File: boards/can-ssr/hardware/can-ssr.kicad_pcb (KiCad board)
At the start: 2 copper layers, 100 x 100 mm, 127 parts, among them J1 CAN IN, J2 CAN OUT, J3 ICSP, J30 MEAN WELL, J4 UART, Q1 IPB110N20N3LF, Q2 IPB110N20N3LF, Q20 2N7002, Q21 2N7002, Q22 2N7002, Q23 2N7002, Q24 2N7002, Q3 IPB110N20N3LF, Q4 IPB110N20N3LF, Q5 MMBT2907A, SW1 ADDR, U1 R-78E5.0-1.0, U10 VOM1271T, U11 VOM1271T, U12 ACS770ECB-100U-PFF-T, U2 MCP2562FD-E/P, U20 LM393B, U3 PIC18F47Q84-I/PT, U30 UCC12050DVE, U31 ISO1640DWR, U32 MCP3426A0-E/SN, U33 MCP4725A0T-E/CH, U34 MCP4725A0T-E/CH, U35 TLP222A, U36 MCP3426A1-E/SN, U40 MAX7219CWG+, U41 CC56-12SRWA, Y1 16MHz

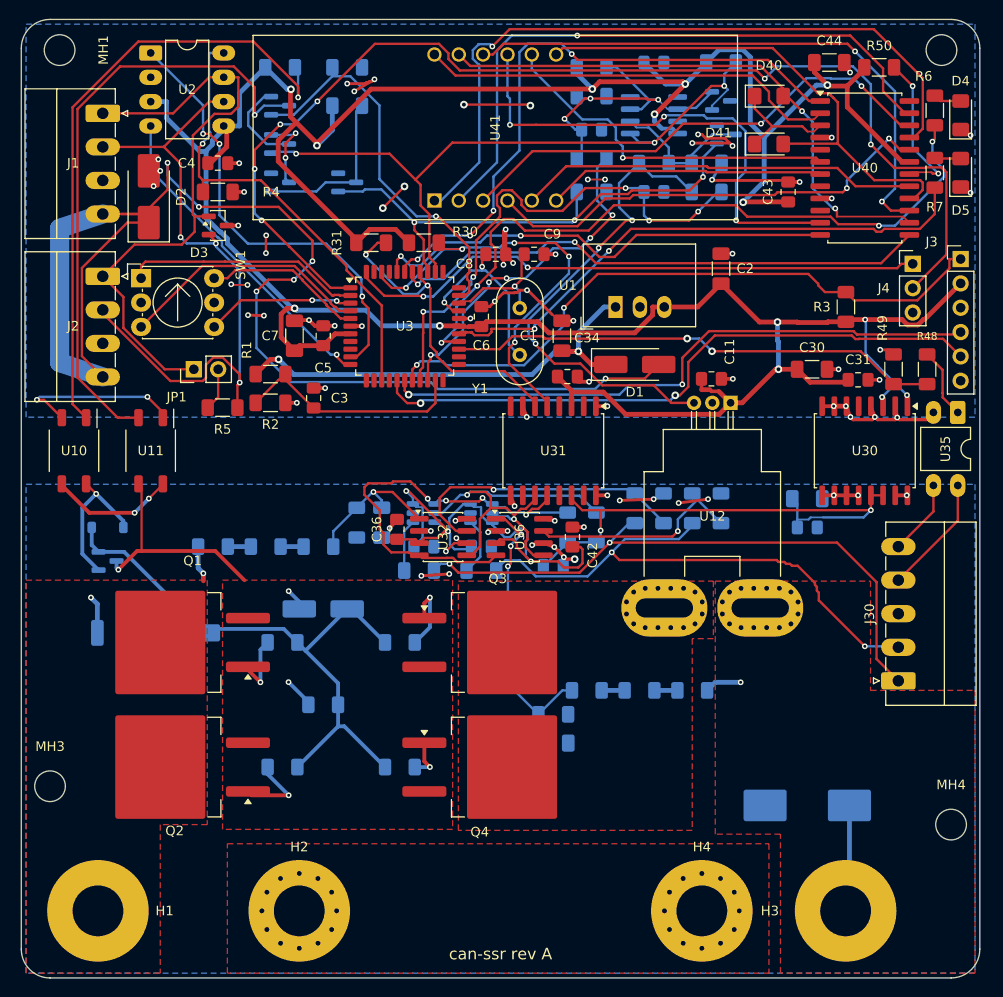
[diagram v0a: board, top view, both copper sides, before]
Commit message: can-ssr: silkscreen labels
- Bolts: SUPPLY +, SUPPLY -, LOAD -, LOAD + (H1-H4 refs hidden);
  NYLON at MH3/MH4 (MH1/MH3 refs hidden to make room)
- Build box BUILD: [ ] HC [ ] STD [ ] HV beside the board name
- Terminal pin names: CAN legend above J1 (shared by J2), Mean Well J30
  (PV, PC, -V, RC, RC), UART J4 (TX, RX, G); UART/ICSP titles, ADDR, TERM,
  V/A indicators
- Isolation barrier: dashed line at y 145 mm on both sides where clear,
  with CAN / LOGIC SIDE and LOAD SIDE - UP TO 200 V
- J4 ref moved below the header; README notes LED meanings
- DRC clean (no silkscreen warnings)

Co-Authored-By: Claude Opus 5.5 <noreply@anthropic.com>
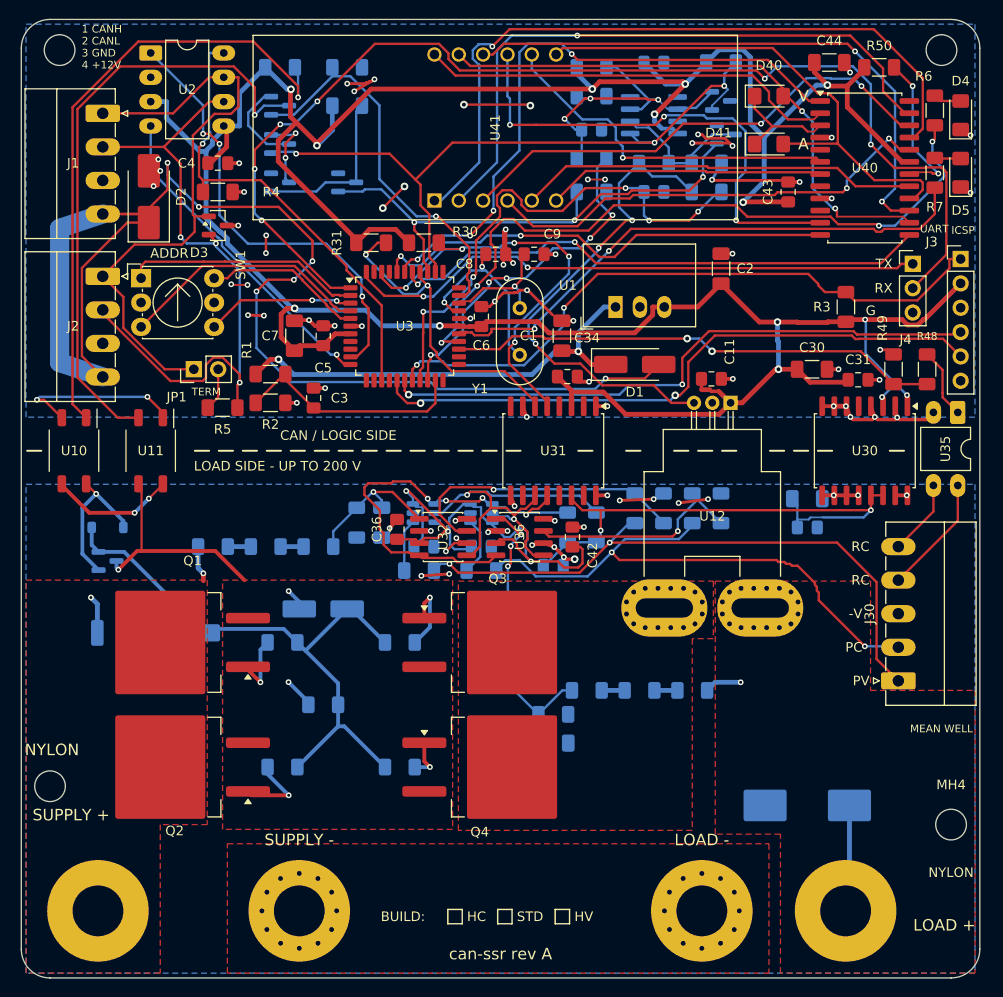
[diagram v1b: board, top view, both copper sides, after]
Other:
- board text added: "-V"
- board text added: "1 CANH"
- board text added: "2 CANL"
- board text added: "3 GND"
- board text added: "4 +12V"
- board text added: "A"
- board text added: "ADDR"
- board text added: "BUILD:"
- board text added: "CAN / LOGIC SIDE"
- board text added: "G"
- board text added: "HC"
- board text added: "HV"
- board text added: "ICSP"
- board text added: "LOAD +"
- board text added: "LOAD -"
- board text added: "LOAD SIDE - UP TO 200 V"
- board text added: "MEAN WELL"
- board text added: "NYLON"
- board text added: "PC"
- board text added: "PV"
- board text added: "RC"
- board text added: "RX"
- board text added: "STD"
- board text added: "SUPPLY +"
- board text added: "SUPPLY -"
- board text added: "TERM"
- board text added: "TX"
- board text added: "UART"
- board text added: "V"

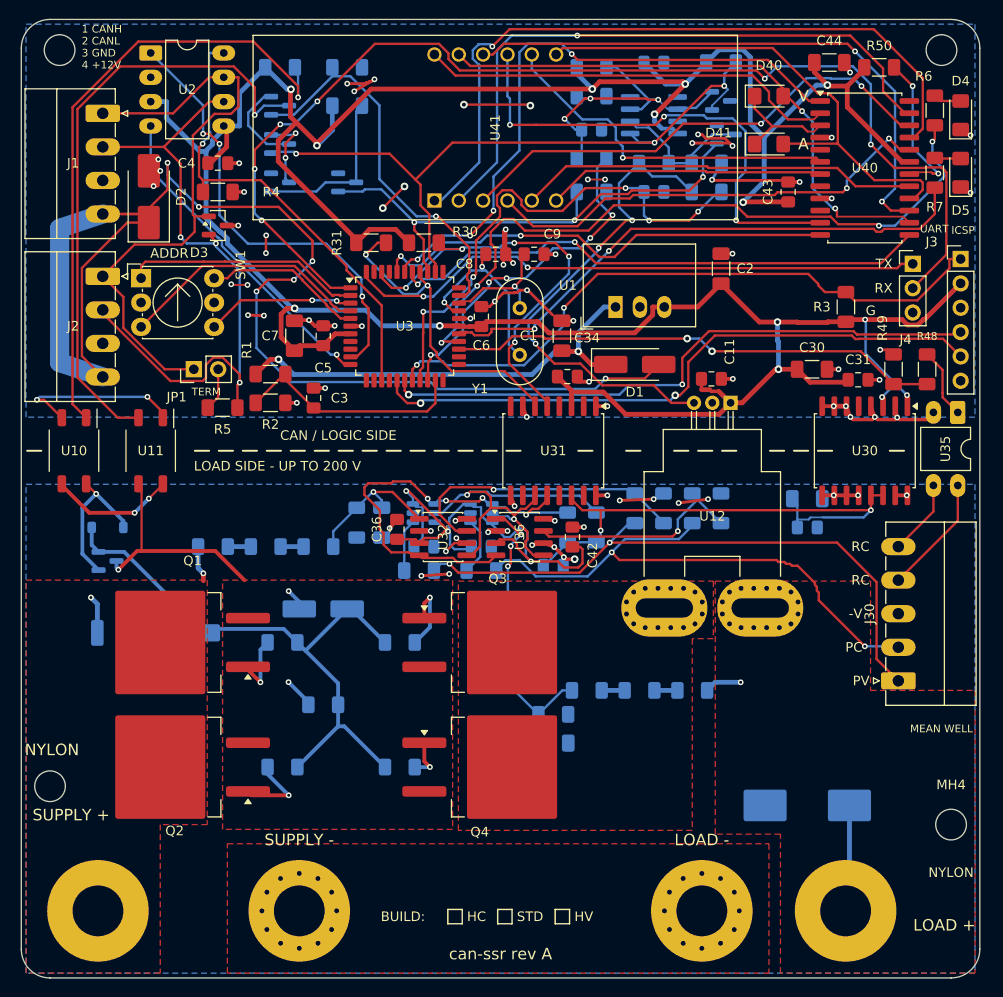
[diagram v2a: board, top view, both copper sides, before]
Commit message: can-ssr: stack interface rework; MCDN double-level CAN header; Ethernet parts
can-ssr (checker clean: ERC, DRC, schematic parity):
- M4 standoff holes 4.5 mm in from each corner (91 x 91 mm), new
  Thl_Mechanical:MountingHole_4.3mm_M4_Standoff7mm (4.3 mm courtyard, both
  sides); copper keep-outs around the load-side holes
- Load bolts moved inward (S+ 18, S- 36, L- 63, L+ 82 mm) with bars, mask
  openings, return bar, pours and labels
- Top-right corner reworked for the MH2 standoff (LED column, R50/C44,
  local reroutes); scoped DRC rule for MH2 beside U40
- CAN IN + CAN OUT -> one Phoenix MCDN 1,5/4-G1-3,5 P26 THR (1953732) at the
  stack CAN position (pin 1 at y 15.5 mm); schematic J1 is Conn_02x04,
  J2 removed; SW1/D2 moved; affected nets rejoined locally
- One-off rework scripts kept in hardware/stack_rework/

Library and tools:
- Footprint generator for the MCDN header (own drawing from Phoenix's
  dimensions); vendor STEP is local-only (SamacSys licence)
- tools/miniroute.py: small two-layer grid router for local rework

Requirements: stack CAN position fixed at pin 1 = 15.5 mm; holes at 4.5 mm;
can-controller Ethernet parts JD0-0004NL jack and HI1206P121R-10 bead (W6100).

Co-Authored-By: Claude Opus 5.5 <noreply@anthropic.com>
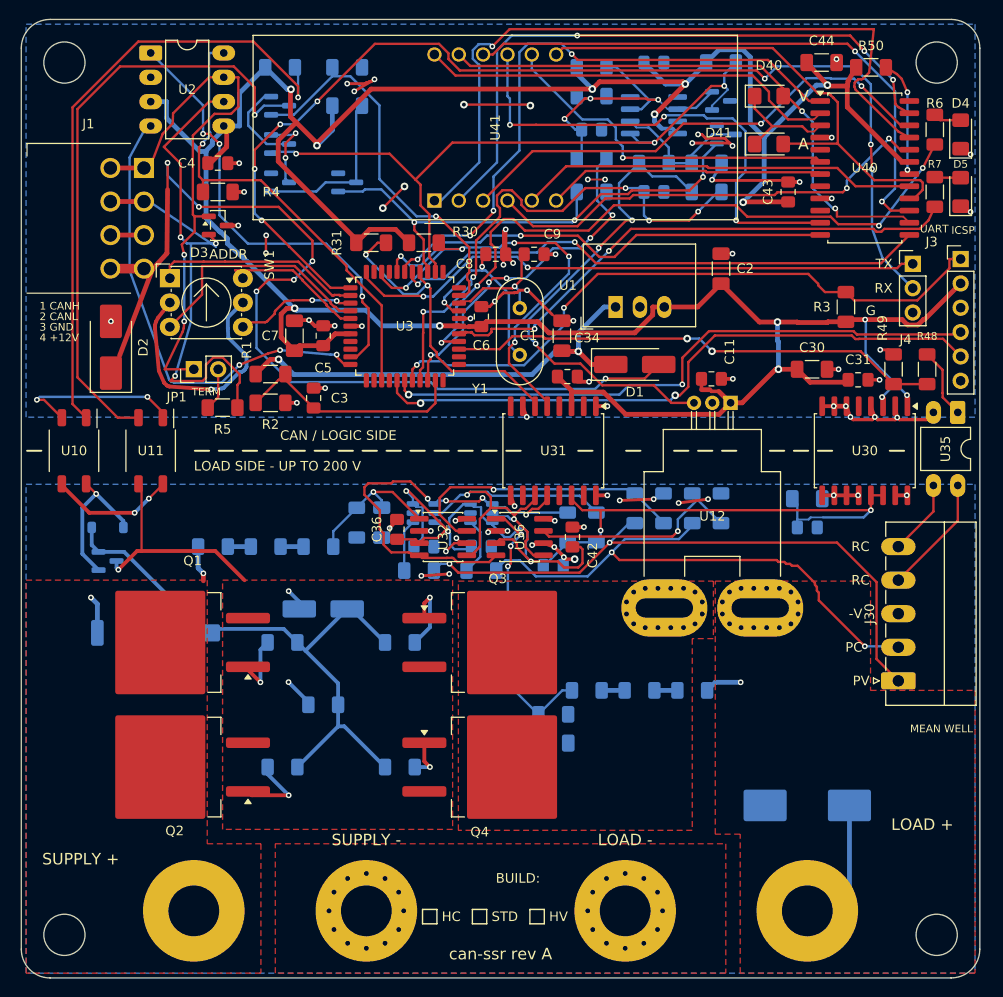
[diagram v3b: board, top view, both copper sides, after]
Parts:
- removed J2: CAN OUT, Connector_Phoenix_MC:PhoenixContact_MC_1,5_4-G-3.5_1x04_P3.50mm_Horizontal
- J1: value CAN IN -> CAN IN/OUT; footprint Connector_Phoenix_MC:PhoenixContact_MC_1,5_4-G-3.5_1x04_P3.50mm_Horizontal -> Thl_Connector:PhoenixContact_MCDN_1,5_4-G1-3,5_2x04_P3.5mm_Horizontal
- MH1, MH2, MH3, MH4: value MountingHole_3.2mm_M3 -> MountingHole_4.3mm_M4_Standoff7mm; footprint MountingHole:MountingHole_3.2mm_M3 -> Thl_Mechanical:MountingHole_4.3mm_M4_Standoff7mm
- moved D2 16.2 mm to (109.3, 134.2)
- moved MH3 15.6 mm to (104.5, 195.5)
- moved MH4 11.6 mm to (195.5, 195.5)
- moved H1 10.0 mm to (118.0, 193.0)
- moved H4 8.00 mm to (163.0, 193.0)
- moved J1 7.14 mm to (112.8, 115.5)
- moved H2 7.00 mm to (136.0, 193.0)
- moved H3 4.00 mm to (182.0, 193.0)
- moved SW1 3.00 mm to (115.5, 127.0)
- moved D4 2.00 mm to (198.0, 112.0)
- moved D5 2.00 mm to (198.0, 118.0)
- moved R6 2.00 mm to (195.3, 111.5)
- moved R7 2.00 mm to (195.3, 118.0)
- moved MH1 1.39 mm to (104.5, 104.5)
- moved MH2 1.39 mm to (195.5, 104.5)
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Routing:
- net /CAN, power, MCU/V12_BUS: track 136.5 -> 104.1 mm
- net GND: track 102.0 -> 125.4 mm, vias 57 -> 52
- net /CAN, power, MCU/CAN_RX: track 34.3 -> 47.5 mm, vias 1 -> 3
- net /CAN, power, MCU/CANH: track 63.3 -> 56.2 mm, vias 0 -> 2
- net /CAN, power, MCU/UART_RX: track 120.8 -> 114.6 mm, vias 6 -> 7
- net /CAN, power, MCU/CANL: track 68.8 -> 63.3 mm
- net /CAN, power, MCU/LED_STATUS: track 74.4 -> 69.9 mm
- net /CAN, power, MCU/ADDR1: track 15.5 -> 11.1 mm
- net /Display/ISET: track 15.9 -> 12.2 mm
- net /CAN, power, MCU/ADDR0: track 24.8 -> 21.8 mm
- net /CAN, power, MCU/LED_FAULT: track 58.6 -> 56.4 mm
- net /CAN, power, MCU/ADDR3: track 16.7 -> 15.3 mm
- net /CAN, power, MCU/ADDR2: track 26.5 -> 25.2 mm
- net /Display/SEG_E: track 75.1 -> 76.1 mm
- net /Display/SEG_D: track 65.3 -> 65.5 mm, vias 1 -> 3
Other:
- board text removed: "NYLON"

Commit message: Probe test points on all fab boards; golden-board R/C/L test tool
tools/testpoints.py puts a 1.0 mm bare-copper pad (Thl_TestPoint:
TP_Probe_D1.0mm, board-only, no silkscreen) on every net of core,
can-card, io-card, serial-card and can-ssr, only on copper the net
already has (track, via or pour): no routing changes. Clear of foreign
copper, courtyards, all silkscreen, isolation gaps; 0.5 mm from the net's
own pads so the probe measures through the joint. Where nothing fits the
probe point is an SMD pad toe. Bottom-side test points where the parts
are on the bottom (can-ssr). DRC loop moves offenders; check_board clean
on all five boards, no reference texts moved or hidden.

tools/tptest.py: plan (net vs domain ground, across two-pin parts,
isolation between ground domains; powered.csv rail checklist) and run
(golden recording, compare with tolerance + golden spread, serial stream
from the planned probe helper or typed values, current.png step map).
docs/probe-test.md describes the workflow and the helper's interface.

Also: silk_tidy --only and board.json silk_keep; io-card place.py places
the AO row references; place.py scripts ignore TP footprints.

Co-Authored-By: Claude Opus 5.5 <noreply@anthropic.com>
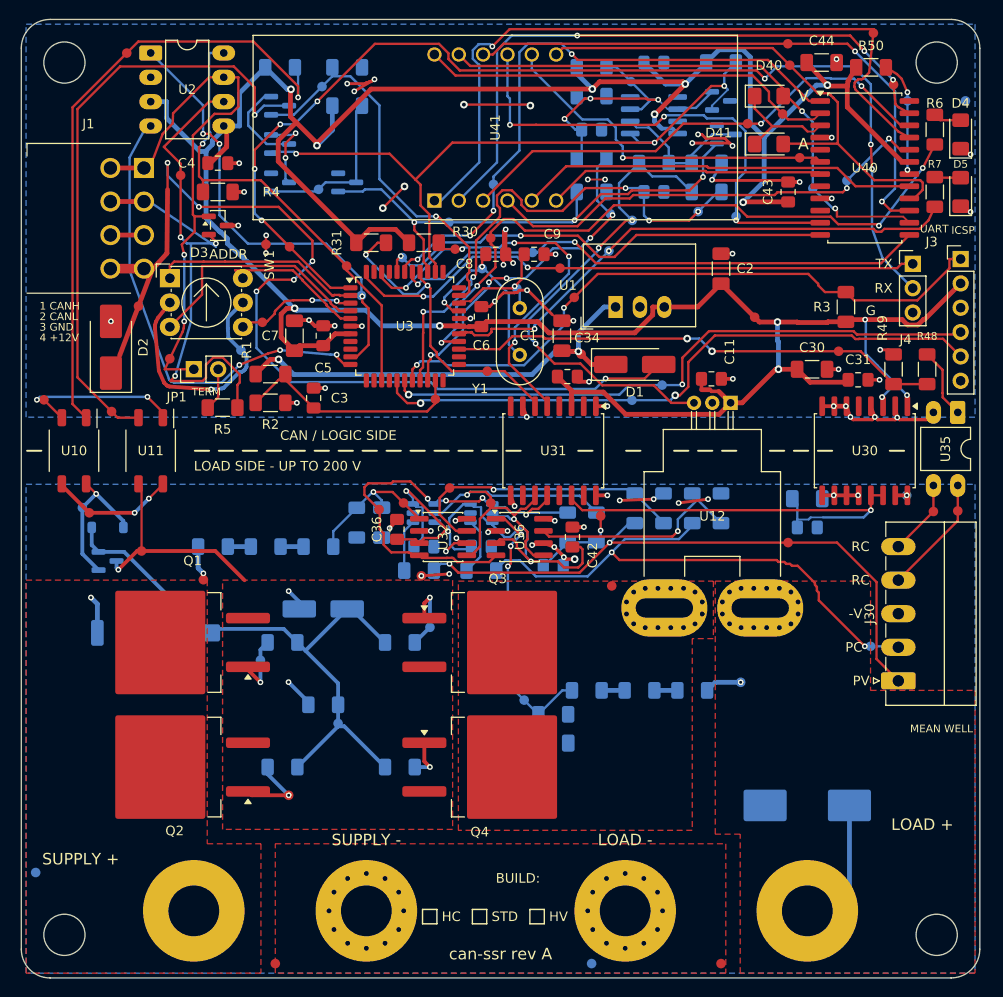
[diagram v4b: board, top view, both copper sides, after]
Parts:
- added TP1: track, Thl_TestPoint:TP_Probe_D1.0mm, F.Cu at (111.0, 103.5)
- added TP10: track, Thl_TestPoint:TP_Probe_D1.0mm, F.Cu at (112.2, 129.9)
- added TP11: track, Thl_TestPoint:TP_Probe_D1.0mm, F.Cu at (125.5, 123.5)
- added TP12: track, Thl_TestPoint:TP_Probe_D1.0mm, F.Cu at (128.0, 123.7)
- added TP13: track, Thl_TestPoint:TP_Probe_D1.0mm, F.Cu at (133.9, 125.7)
- added TP14: track, Thl_TestPoint:TP_Probe_D1.0mm, F.Cu at (145.3, 124.0)
- added TP15: track, Thl_TestPoint:TP_Probe_D1.0mm, F.Cu at (149.0, 122.8)
- added TP16: track, Thl_TestPoint:TP_Probe_D1.0mm, F.Cu at (156.2, 126.0)
- added TP17: track, Thl_TestPoint:TP_Probe_D1.0mm, F.Cu at (157.7, 129.0)
- added TP18: track, Thl_TestPoint:TP_Probe_D1.0mm, F.Cu at (102.4, 139.7)
- added TP19: track, Thl_TestPoint:TP_Probe_D1.0mm, F.Cu at (115.5, 135.4)
- added TP2: track, Thl_TestPoint:TP_Probe_D1.0mm, F.Cu at (179.4, 109.9)
- added TP20: track, Thl_TestPoint:TP_Probe_D1.0mm, F.Cu at (125.2, 131.6)
- added TP21: track, Thl_TestPoint:TP_Probe_D1.0mm, F.Cu at (143.2, 139.6)
- added TP22: track, Thl_TestPoint:TP_Probe_D1.0mm, F.Cu at (148.6, 136.7)
- added TP23: track, Thl_TestPoint:TP_Probe_D1.0mm, F.Cu at (158.4, 134.9)
- added TP24: track, Thl_TestPoint:TP_Probe_D1.0mm, F.Cu at (176.5, 131.1)
- added TP25: track, Thl_TestPoint:TP_Probe_D1.0mm, F.Cu at (185.3, 134.6)
- added TP26: track, Thl_TestPoint:TP_Probe_D1.0mm, F.Cu at (109.4, 140.9)
- added TP27: track, Thl_TestPoint:TP_Probe_D1.0mm, F.Cu at (144.7, 148.9)
- added TP28: track, Thl_TestPoint:TP_Probe_D1.0mm, F.Cu at (107.1, 151.5)
- added TP29: track, Thl_TestPoint:TP_Probe_D1.0mm, F.Cu at (112.5, 155.5)
- added TP3: track, Thl_TestPoint:TP_Probe_D1.0mm, F.Cu at (180.0, 102.5)
- added TP30: track, Thl_TestPoint:TP_Probe_D1.0mm, F.Cu at (119.0, 158.5)
- added TP31: track, Thl_TestPoint:TP_Probe_D1.0mm, F.Cu at (137.3, 151.1)
- added TP32: track, Thl_TestPoint:TP_Probe_D1.0mm, F.Cu at (139.9, 150.4)
- added TP33: track, Thl_TestPoint:TP_Probe_D1.0mm, F.Cu at (141.7, 158.1)
- added TP34: track, Thl_TestPoint:TP_Probe_D1.0mm, F.Cu at (149.0, 150.4)
- added TP35: track, Thl_TestPoint:TP_Probe_D1.0mm, F.Cu at (160.4, 151.8)
- added TP36: pour, Thl_TestPoint:TP_Probe_D1.0mm, F.Cu at (161.6, 159.1)
- added TP37: track, Thl_TestPoint:TP_Probe_D1.0mm, F.Cu at (180.0, 154.6)
- added TP38: track, Thl_TestPoint:TP_Probe_D1.0mm, F.Cu at (195.2, 151.3)
- added TP39: track, Thl_TestPoint:TP_Probe_D1.0mm, F.Cu at (197.7, 151.3)
- added TP4: track, Thl_TestPoint:TP_Probe_D1.0mm, F.Cu at (180.2, 104.8)
- added TP40: track, Thl_TestPoint:TP_Probe_D1.0mm, F.Cu at (127.9, 180.9)
- added TP41: pour, Thl_TestPoint:TP_Probe_D1.0mm, F.Cu at (126.5, 198.5)
- added TP42: pour, Thl_TestPoint:TP_Probe_D1.0mm, F.Cu at (173.0, 198.5)
- added TP43: pour, Thl_TestPoint:TP_Probe_D1.0mm, B.Cu at (198.5, 108.5)
- added TP44: track, Thl_TestPoint:TP_Probe_D1.0mm, B.Cu at (192.4, 108.5)
- added TP45: track, Thl_TestPoint:TP_Probe_D1.0mm, B.Cu at (163.6, 106.5)
- added TP46: track, Thl_TestPoint:TP_Probe_D1.0mm, B.Cu at (131.4, 107.0)
- added TP47: track, Thl_TestPoint:TP_Probe_D1.0mm, B.Cu at (186.1, 116.8)
- added TP48: track, Thl_TestPoint:TP_Probe_D1.0mm, B.Cu at (182.6, 117.6)
- added TP49: track, Thl_TestPoint:TP_Probe_D1.0mm, B.Cu at (149.3, 117.2)
- added TP5: track, Thl_TestPoint:TP_Probe_D1.0mm, F.Cu at (188.9, 101.4)
- added TP50: track, Thl_TestPoint:TP_Probe_D1.0mm, B.Cu at (131.0, 117.7)
- added TP51: track, Thl_TestPoint:TP_Probe_D1.0mm, B.Cu at (174.6, 120.6)
- added TP52: track, Thl_TestPoint:TP_Probe_D1.0mm, B.Cu at (170.6, 120.0)
- added TP53: track, Thl_TestPoint:TP_Probe_D1.0mm, B.Cu at (163.7, 121.0)
- added TP54: track, Thl_TestPoint:TP_Probe_D1.0mm, B.Cu at (161.4, 120.3)
- added TP55: track, Thl_TestPoint:TP_Probe_D1.0mm, B.Cu at (161.3, 124.2)
- added TP56: track, Thl_TestPoint:TP_Probe_D1.0mm, B.Cu at (153.3, 124.3)
- added TP57: track, Thl_TestPoint:TP_Probe_D1.0mm, B.Cu at (151.7, 128.1)
- added TP58: track, Thl_TestPoint:TP_Probe_D1.0mm, B.Cu at (148.1, 126.0)
- added TP59: track, Thl_TestPoint:TP_Probe_D1.0mm, B.Cu at (144.6, 121.2)
- added TP6: track, Thl_TestPoint:TP_Probe_D1.0mm, F.Cu at (191.0, 106.8)
- added TP60: track, Thl_TestPoint:TP_Probe_D1.0mm, B.Cu at (139.7, 124.8)
- added TP61: track, Thl_TestPoint:TP_Probe_D1.0mm, B.Cu at (135.5, 128.8)
- added TP62: track, Thl_TestPoint:TP_Probe_D1.0mm, B.Cu at (166.9, 138.2)
- added TP63: track, Thl_TestPoint:TP_Probe_D1.0mm, B.Cu at (163.7, 139.7)
- added TP64: track, Thl_TestPoint:TP_Probe_D1.0mm, B.Cu at (128.2, 134.6)
- added TP65: track, Thl_TestPoint:TP_Probe_D1.0mm, B.Cu at (122.9, 134.5)
- added TP66: via, Thl_TestPoint:TP_Probe_D1.0mm, B.Cu at (192.4, 149.7)
- added TP67: track, Thl_TestPoint:TP_Probe_D1.0mm, B.Cu at (106.4, 150.9)
- added TP68: track, Thl_TestPoint:TP_Probe_D1.0mm, B.Cu at (188.6, 165.4)
- added TP69: track, Thl_TestPoint:TP_Probe_D1.0mm, B.Cu at (175.1, 169.2)
- added TP7: track, Thl_TestPoint:TP_Probe_D1.0mm, F.Cu at (116.6, 116.3)
- added TP70: track, Thl_TestPoint:TP_Probe_D1.0mm, B.Cu at (142.6, 163.4)
- added TP71: track, Thl_TestPoint:TP_Probe_D1.0mm, B.Cu at (125.0, 166.9)
- added TP72: track, Thl_TestPoint:TP_Probe_D1.0mm, B.Cu at (152.5, 171.0)
- added TP73: track, Thl_TestPoint:TP_Probe_D1.0mm, B.Cu at (133.1, 173.4)
- added TP74: pour, Thl_TestPoint:TP_Probe_D1.0mm, B.Cu at (101.5, 189.0)
- added TP75: pour, Thl_TestPoint:TP_Probe_D1.0mm, B.Cu at (159.5, 198.5)
- added TP8: track, Thl_TestPoint:TP_Probe_D1.0mm, F.Cu at (175.8, 110.9)
- added TP9: track, Thl_TestPoint:TP_Probe_D1.0mm, F.Cu at (181.2, 114.4)
